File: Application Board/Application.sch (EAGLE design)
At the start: 57 parts, among them Q1 DMP2012SN-7, T1 FDN340P, T2 AP1117_LIN_REG, U1 LM3409HV'LM3409HV'

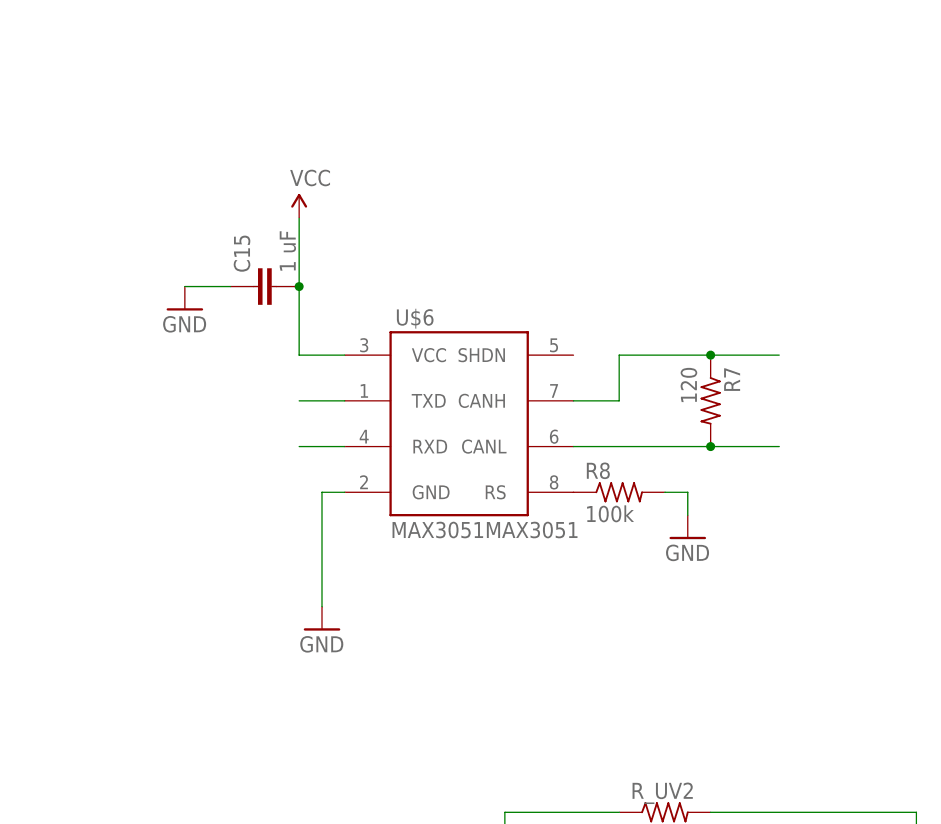
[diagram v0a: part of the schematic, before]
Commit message: Moved capacitors around
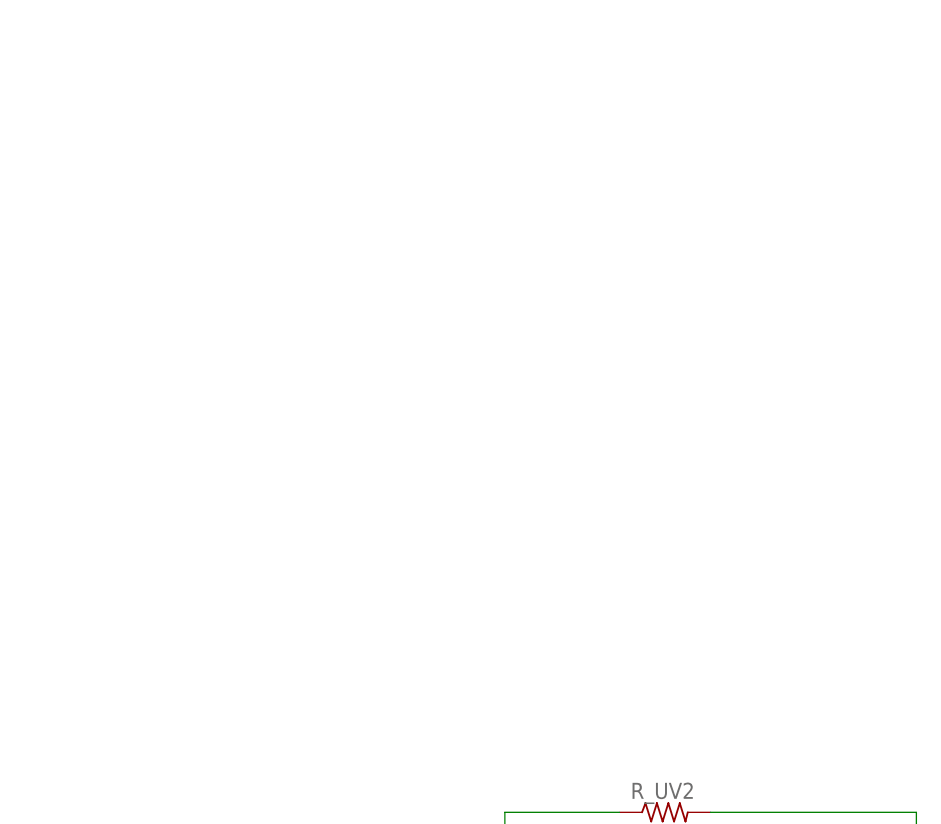
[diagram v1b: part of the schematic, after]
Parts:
- removed C15: 1 uF, capacitor-wima:C2,5-3
- removed R7: 120, resistor:R-US_0204/2V
- removed R8: 100k, resistor:R-US_0204/2V
- removed U$6: MAX3051MAX3051, MAX3051 Library:MAX3051MAX3051
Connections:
- removed net CANH1: R7.1, U$6.CANH
- removed net CANL1: R7.2, U$6.CANL
- removed net N$19: R8.1, U$6.RS
- removed net RXD: U$6.RXD
- removed net TXD: U$6.TXD
- removed net VCC: C15.2, U$6.VCC
- net GND: no longer C15.1, R8.2, U$6.GND
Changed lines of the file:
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@@
 <?xml version="1.0" encoding="utf-8"?>
 <!DOCTYPE eagle SYSTEM "eagle.dtd">
-<eagle version="6.5.0">
+<eagle version="7.5.0">
 <drawing>
 <settings>
@@
 <setting verticaltext="up"/>
 </settings>
-<grid distance="0.05" unitdist="inch" unit="inch" style="lines" multiple="1" display="yes" altdistance="0.005" altunitdist="inch" altunit="inch"/>
+<grid distance="0.1" unitdist="inch" unit="inch" style="lines" multiple="1" display="no" altdistance="0.01" altunitdist="inch" altunit="inch"/>
 <layers>
 <layer number="1" name="Top" color="4" fill="1" visible="no" active="no"/>
@@
 <part name="GND17" library="supply1" deviceset="GND" device=""/>
 <part name="U1" library="2015_LED_Driver" deviceset="LM3409HV" device="'LM3409HV'"/>
-<part name="U$6" library="MAX3051 Library" deviceset="MAX3051" device="MAX3051"/>
-<part name="C15" library="capacitor-wima" deviceset="C" device="2,5-3" value="1 uF"/>
-<part name="R7" library="resistor" deviceset="R-US_" device="0204/2V" value="120"/>
-<part name="R8" library="resistor" deviceset="R-US_" device="0204/2V" value="100k"/>
-<part name="SUPPLY1" library="SparkFun-Aesthetics" deviceset="VCC" device=""/>
-<part name="GND18" library="SparkFun-Aesthetics" deviceset="GND" device=""/>
-<part name="GND19" library="SparkFun-Aesthetics" deviceset="GND" device=""/>
-<part name="GND20" library="SparkFun-Aesthetics" deviceset="GND" device=""/>
 <part name="FRAME3" library="frames" deviceset="FRAME_A_L" device=""/>
 </parts>
@@
 <instance part="+3V7" gate="G$1" x="373.38" y="149.86"/>
 <instance part="GND11" gate="1" x="353.06" y="124.46"/>
-<instance part="U$6" gate="G$1" x="33.02" y="-72.39"/>
-<instance part="C15" gate="G$1" x="10.16" y="-57.15" rot="R90"/>
-<instance part="R7" gate="G$1" x="60.96" y="-69.85" rot="R270"/>
-<instance part="R8" gate="G$1" x="50.8" y="-80.01"/>
-<instance part="SUPPLY1" gate="G$1" x="15.24" y="-49.53"/>
-<instance part="GND18" gate="1" x="17.78" y="-95.25"/>
-<instance part="GND19" gate="1" x="58.42" y="-85.09"/>
-<instance part="GND20" gate="1" x="2.54" y="-59.69"/>
 <instance part="R_UV2" gate="G$1" x="55.88" y="-115.57"/>
 <instance part="R_UV1" gate="G$1" x="30.48" y="-123.19"/>
@@
 </segment>
 <segment>
-<pinref part="U$6" gate="G$1" pin="GND"/>
-<wire x1="20.32" y1="-80.01" x2="17.78" y2="-80.01" width="0.1524" layer="91"/>
-<wire x1="17.78" y1="-80.01" x2="17.78" y2="-92.71" width="0.1524" layer="91"/>
-<pinref part="GND18" gate="1" pin="GND"/>
-</segment>
-<segment>
-<pinref part="R8" gate="G$1" pin="2"/>
-<wire x1="55.88" y1="-80.01" x2="58.42" y2="-80.01" width="0.1524" layer="91"/>
-<wire x1="58.42" y1="-80.01" x2="58.42" y2="-82.55" width="0.1524" layer="91"/>
-<pinref part="GND19" gate="1" pin="GND"/>
-</segment>
-<segment>
-<pinref part="C15" gate="G$1" pin="1"/>
-<wire x1="2.54" y1="-57.15" x2="7.62" y2="-57.15" width="0.1524" layer="91"/>
-<pinref part="GND20" gate="1" pin="GND"/>
-</segment>
-<segment>
 <pinref part="C_IN2" gate="G$1" pin="2"/>
 <pinref part="GND14" gate="1" pin="GND"/>
@@
 </segment>
 </net>
-<net name="N$19" class="0">
-<segment>
-<pinref part="U$6" gate="G$1" pin="RS"/>
-<pinref part="R8" gate="G$1" pin="1"/>
-</segment>
-</net>
-<net name="VCC" class="0">
-<segment>
-<pinref part="U$6" gate="G$1" pin="VCC"/>
-<pinref part="SUPPLY1" gate="G$1" pin="VCC"/>
-<wire x1="20.32" y1="-64.77" x2="15.24" y2="-64.77" width="0.1524" layer="91"/>
-<wire x1="15.24" y1="-64.77" x2="15.24" y2="-57.15" width="0.1524" layer="91"/>
-<pinref part="C15" gate="G$1" pin="2"/>
-<wire x1="15.24" y1="-57.15" x2="15.24" y2="-49.53" width="0.1524" layer="91"/>
-<junction x="15.24" y="-57.15"/>
-</segment>
-</net>
-<net name="CANL1" class="0">
-<segment>
-<pinref part="U$6" gate="G$1" pin="CANL"/>
-<wire x1="45.72" y1="-74.93" x2="60.96" y2="-74.93" width="0.1524" layer="91"/>
-<pinref part="R7" gate="G$1" pin="2"/>
-<wire x1="60.96" y1="-74.93" x2="68.58" y2="-74.93" width="0.1524" layer="91"/>
-<junction x="60.96" y="-74.93"/>
-</segment>
-</net>
-<net name="CANH1" class="0">
-<segment>
-<pinref part="R7" gate="G$1" pin="1"/>
-<wire x1="60.96" y1="-64.77" x2="50.8" y2="-64.77" width="0.1524" layer="91"/>
-<wire x1="50.8" y1="-64.77" x2="50.8" y2="-69.85" width="0.1524" layer="91"/>
-<pinref part="U$6" gate="G$1" pin="CANH"/>
-<wire x1="50.8" y1="-69.85" x2="45.72" y2="-69.85" width="0.1524" layer="91"/>
-<wire x1="60.96" y1="-64.77" x2="68.58" y2="-64.77" width="0.1524" layer="91"/>
-<junction x="60.96" y="-64.77"/>
-</segment>
-</net>
-<net name="TXD" class="0">
-<segment>
-<pinref part="U$6" gate="G$1" pin="TXD"/>
-<wire x1="20.32" y1="-69.85" x2="15.24" y2="-69.85" width="0.1524" layer="91"/>
-</segment>
-</net>
-<net name="RXD" class="0">
-<segment>
-<pinref part="U$6" gate="G$1" pin="RXD"/>
-<wire x1="20.32" y1="-74.93" x2="15.24" y2="-74.93" width="0.1524" layer="91"/>
-</segment>
-</net>

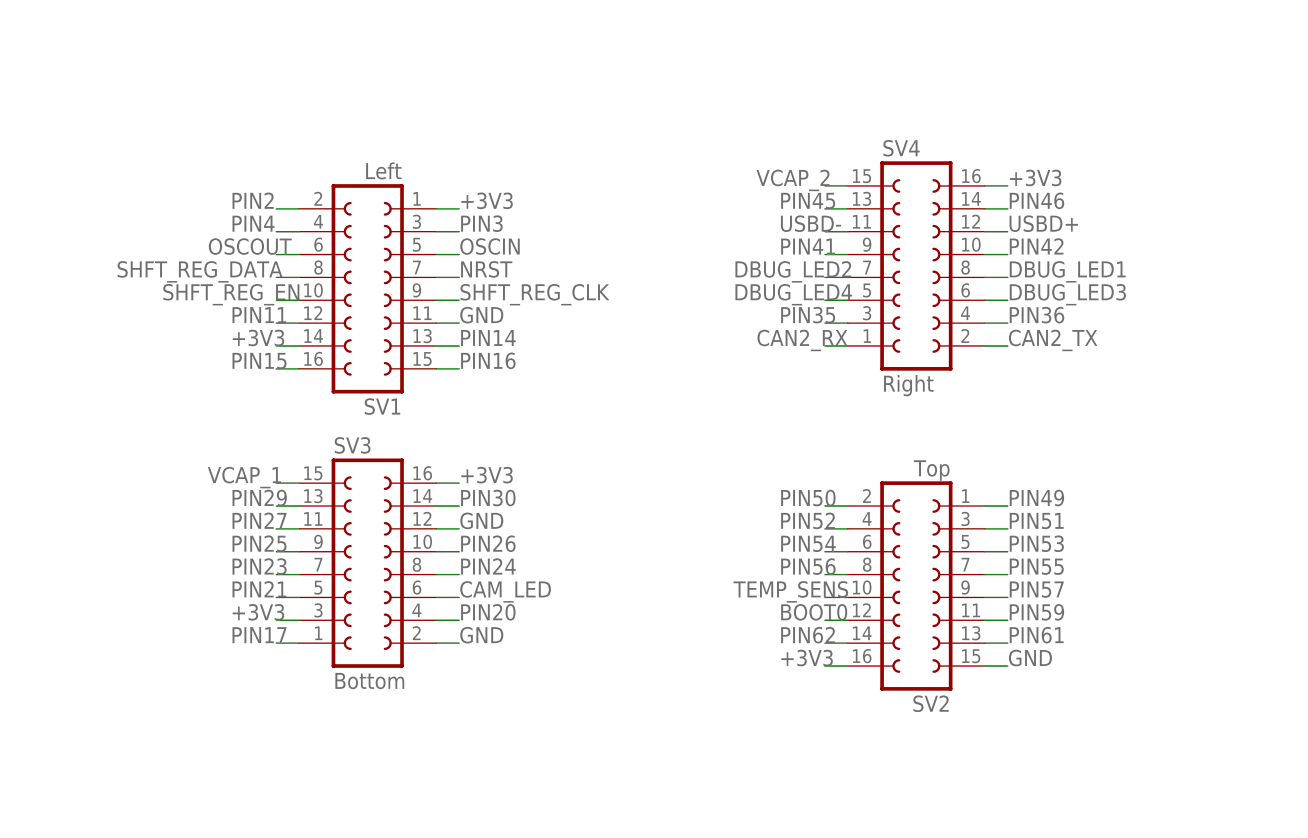
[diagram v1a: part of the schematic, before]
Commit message: Fixed all the routing on the microcontroller.
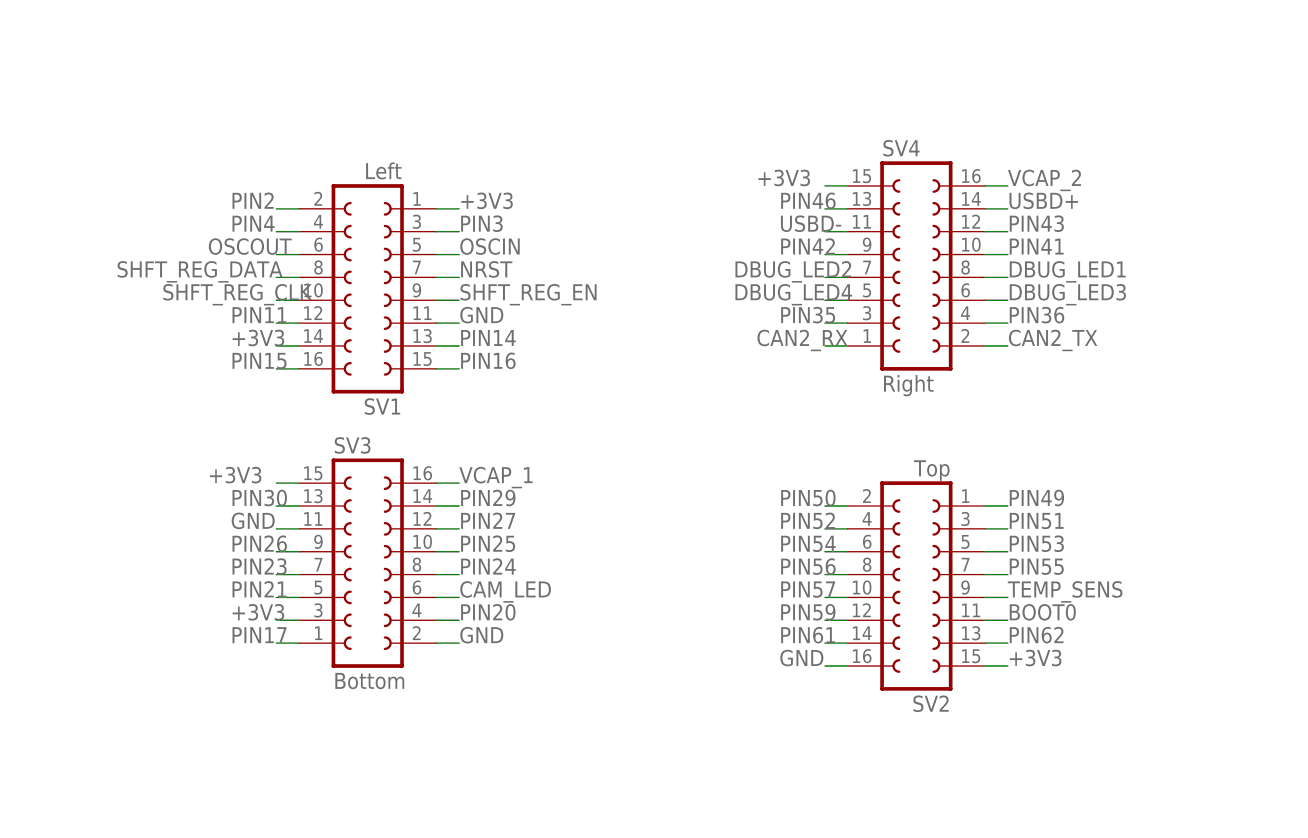
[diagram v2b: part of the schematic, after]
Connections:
- removed net PIN45: SV4.13
- net +3V3: now also SV2.15, SV3.15, SV4.15; no longer SV2.16, SV3.16, SV4.16
- net BOOT0: now also SV2.11; no longer SV2.12
- net GND: now also SV2.16, SV3.11; no longer SV2.15, SV3.12
- net PIN25: now also SV3.10; no longer SV3.9
- net PIN26: now also SV3.9; no longer SV3.10
- net PIN27: now also SV3.12; no longer SV3.11
- net PIN29: now also SV3.14; no longer SV3.13
- net PIN30: now also SV3.13; no longer SV3.14
- net PIN41: now also SV4.10; no longer SV4.9
- net PIN42: now also SV4.9; no longer SV4.10
- net PIN43: now also SV4.12
- net PIN46: now also SV4.13; no longer SV4.14
- net PIN57: now also SV2.10; no longer SV2.9
- net PIN59: now also SV2.12; no longer SV2.11
- net PIN61: now also SV2.14; no longer SV2.13
- net PIN62: now also SV2.13; no longer SV2.14
- net SHFT_REG_CLK: now also SV1.10; no longer SV1.9
- net SHFT_REG_EN: now also SV1.9; no longer SV1.10
- net TEMP_SENS: now also SV2.9; no longer SV2.10
- net USBD+: now also SV4.14; no longer SV4.12
- net VCAP_1: now also SV3.16; no longer SV3.15
- net VCAP_2: now also SV4.16; no longer SV4.15

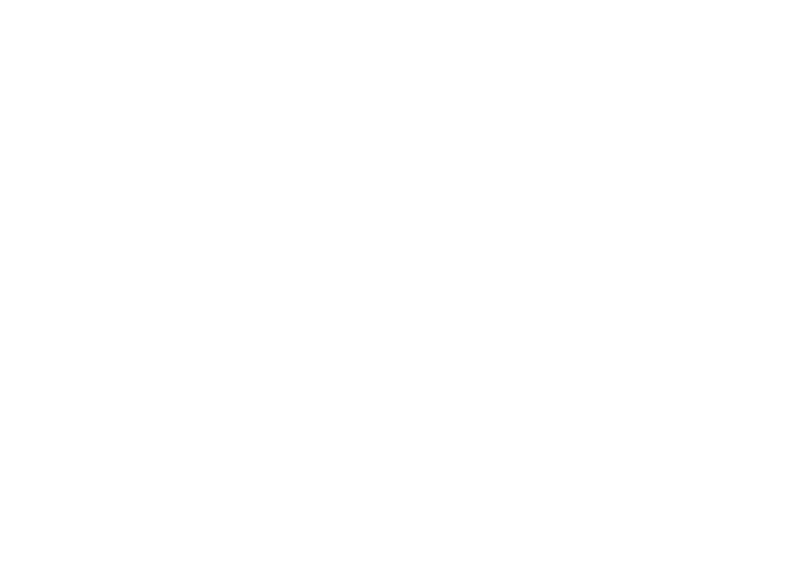
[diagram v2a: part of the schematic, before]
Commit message: added order of board input voltage and signals
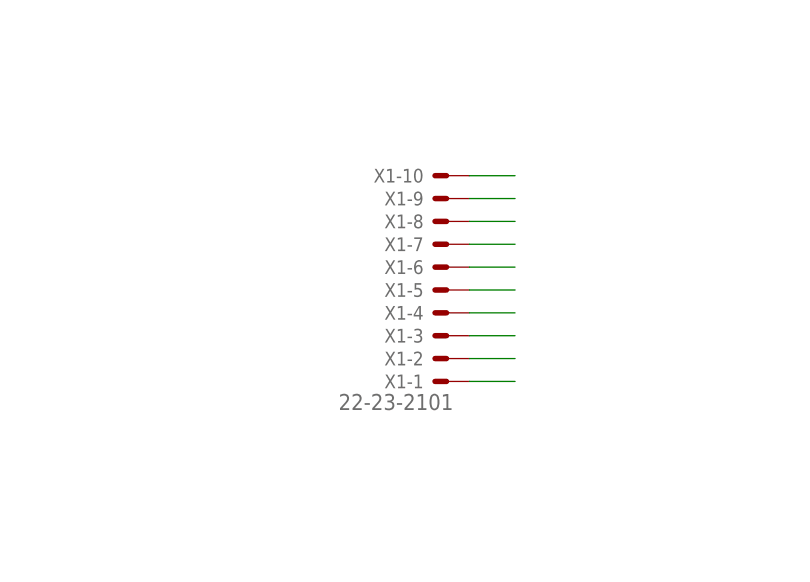
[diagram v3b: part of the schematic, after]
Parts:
- added X1: 22-23-2101, con-molex:22-23-2101
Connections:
- new net 12V: X1-10.S
- net +5V: now also X1-9.S
- net CAM_LED: now also X1-1.S
- net CANH: now also X1-7.S
- net CANL: now also X1-6.S
- net GND: now also X1-8.S
- net SHFT_REG_CLK: now also X1-3.S
- net SHFT_REG_DATA: now also X1-4.S
- net SHFT_REG_EN: now also X1-2.S
- net TEMP_SENS: now also X1-5.S
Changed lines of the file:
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@@
 <part name="U1" library="2015_LED_Driver" deviceset="LM3409HV" device="'LM3409HV'"/>
 <part name="FRAME3" library="frames" deviceset="FRAME_A_L" device=""/>
+<part name="X1" library="con-molex" deviceset="22-23-2101" device=""/>
 </parts>
 <sheets>
@@
 <instance part="FRAME3" gate="G$1" x="-27.94" y="-243.84"/>
 <instance part="FRAME3" gate="G$2" x="139.7" y="-243.84"/>
+<instance part="X1" gate="-1" x="180.34" y="-121.92" rot="R180"/>
+<instance part="X1" gate="-2" x="180.34" y="-119.38" rot="R180"/>
+<instance part="X1" gate="-3" x="180.34" y="-116.84" rot="R180"/>
+<instance part="X1" gate="-4" x="180.34" y="-114.3" rot="R180"/>
+<instance part="X1" gate="-5" x="180.34" y="-111.76" rot="R180"/>
+<instance part="X1" gate="-6" x="180.34" y="-109.22" rot="R180"/>
+<instance part="X1" gate="-7" x="180.34" y="-106.68" rot="R180"/>
+<instance part="X1" gate="-8" x="180.34" y="-104.14" rot="R180"/>
+<instance part="X1" gate="-9" x="180.34" y="-101.6" rot="R180"/>
+<instance part="X1" gate="-10" x="180.34" y="-99.06" rot="R180"/>
 </instances>
 <busses>
@@
 <label x="81.28" y="12.7" size="1.778" layer="95"/>
 </segment>
+<segment>
+<pinref part="X1" gate="-8" pin="S"/>
+<wire x1="182.88" y1="-104.14" x2="187.96" y2="-104.14" width="0.1524" layer="91"/>
+</segment>
 </net>
 <net name="OSCIN" class="0">
@@
 <junction x="322.58" y="152.4"/>
 </segment>
+<segment>
+<pinref part="X1" gate="-9" pin="S"/>
+<wire x1="182.88" y1="-101.6" x2="187.96" y2="-101.6" width="0.1524" layer="91"/>
+</segment>
 </net>
 <net name="N$58" class="0">
@@
 <label x="490.22" y="134.62" size="1.778" layer="95"/>
 </segment>
+<segment>
+<pinref part="X1" gate="-6" pin="S"/>
+<wire x1="182.88" y1="-109.22" x2="187.96" y2="-109.22" width="0.1524" layer="91"/>
+</segment>
 </net>
 <net name="CANH" class="0">
@@
 <label x="490.22" y="144.78" size="1.778" layer="95"/>
 </segment>
+<segment>
+<pinref part="X1" gate="-7" pin="S"/>
+<wire x1="182.88" y1="-106.68" x2="187.96" y2="-106.68" width="0.1524" layer="91"/>
+</segment>
 </net>
 <net name="N$63" class="0">
@@
 <label x="7.62" y="55.88" size="1.778" layer="95"/>
 </segment>
+<segment>
+<pinref part="X1" gate="-4" pin="S"/>
+<wire x1="182.88" y1="-114.3" x2="187.96" y2="-114.3" width="0.1524" layer="91"/>
+</segment>
 </net>
 <net name="SHFT_REG_CLK" class="0">
@@
 <label x="12.7" y="53.34" size="1.778" layer="95"/>
 </segment>
+<segment>
+<pinref part="X1" gate="-3" pin="S"/>
+<wire x1="182.88" y1="-116.84" x2="187.96" y2="-116.84" width="0.1524" layer="91"/>
+</segment>
 </net>
 <net name="SHFT_REG_EN" class="0">
@@
 <label x="45.72" y="53.34" size="1.778" layer="95"/>
 </segment>
+<segment>
+<pinref part="X1" gate="-2" pin="S"/>
+<wire x1="182.88" y1="-119.38" x2="187.96" y2="-119.38" width="0.1524" layer="91"/>
+</segment>
 </net>
 <net name="CAM_LED" class="0">
@@
 <label x="45.72" y="20.32" size="1.778" layer="95"/>
 </segment>
+<segment>
+<pinref part="X1" gate="-1" pin="S"/>
+<wire x1="182.88" y1="-121.92" x2="187.96" y2="-121.92" width="0.1524" layer="91"/>
+</segment>
 </net>
 <net name="CAN2_RX" class="0">
@@
 <wire x1="104.14" y1="20.32" x2="106.68" y2="20.32" width="0.1524" layer="91"/>
 <label x="106.68" y="20.32" size="1.778" layer="95"/>
+</segment>
+<segment>
+<pinref part="X1" gate="-5" pin="S"/>
+<wire x1="182.88" y1="-111.76" x2="187.96" y2="-111.76" width="0.1524" layer="91"/>
 </segment>
 </net>
@@
 </segment>
 </net>
+<net name="12V" class="0">
+<segment>
+<pinref part="X1" gate="-10" pin="S"/>
+<wire x1="182.88" y1="-99.06" x2="187.96" y2="-99.06" width="0.1524" layer="91"/>
+</segment>
+</net>
